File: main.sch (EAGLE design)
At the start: 12 parts, among them IC1 4001N, IC2 4069N, IC3 ISO1050DUB, IC4 ISO1050DUB, IC5 LD117AV33

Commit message: Pin pitch of TI's MSP430 N20 package now aligns with grid
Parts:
- renumbered 5V to VIN
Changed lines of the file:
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@@
 <part name="P+5" library="supply1" deviceset="VCC" device=""/>
 <part name="GND3" library="supply1" deviceset="GND" device=""/>
-<part name="5V" library="pinhead" deviceset="PINHD-1X2" device=""/>
+<part name="VIN" library="pinhead" deviceset="PINHD-1X2" device=""/>
 <part name="GND8" library="supply1" deviceset="GND" device=""/>
 <part name="GND10" library="supply1" deviceset="GND" device=""/>
@@
 <instance part="P+5" gate="VCC" x="48.26" y="78.74" rot="R180"/>
 <instance part="GND3" gate="1" x="48.26" y="91.44" rot="R180"/>
-<instance part="5V" gate="G$1" x="5.08" y="53.34" rot="R180"/>
+<instance part="VIN" gate="G$1" x="5.08" y="53.34" rot="R180"/>
 <instance part="GND8" gate="1" x="7.62" y="43.18"/>
 <instance part="IC2" gate="E" x="106.68" y="101.6" rot="R180"/>
@@
 </segment>
 <segment>
-<pinref part="5V" gate="G$1" pin="1"/>
+<pinref part="VIN" gate="G$1" pin="1"/>
 <pinref part="GND8" gate="1" pin="GND"/>
 <wire x1="7.62" y1="45.72" x2="7.62" y2="50.8" width="0.1524" layer="91"/>
@@
 <wire x1="15.24" y1="53.34" x2="17.78" y2="53.34" width="0.1524" layer="91"/>
 <junction x="15.24" y="53.34"/>
-<pinref part="5V" gate="G$1" pin="2"/>
-</segment>
-</net>
+<pinref part="VIN" gate="G$1" pin="2"/>
+</segment>
+</net>

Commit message: Replaced MSP430 with correct IC (MSP430G2553), improved board annotations, and added parts list to README
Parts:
- removed MSP430: G2X[0/3]2---N20, TI_MSP430_v16:G2X[0/3]2---N20
- added MSP430G2553: G2XX3---N20, TI_MSP430_v16:G2XX3---N20
- C1: value 100nf -> 0.1uF
- C2: value 10uf -> 10uF
- renumbered C3 to C1, C4 to C2, IC1 to RON, IC2 to VNI, IC3 to HVISO, IC4 to LVISO
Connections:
- net GND: now also MSP430G2553.20; no longer MSP430.20
- net N$1: now also MSP430G2553.16; no longer MSP430.16
- net N$2: now also MSP430G2553.17; no longer MSP430.17
- net N$21: now also MSP430G2553.8; no longer MSP430.8
- net N$22: now also MSP430G2553.13; no longer MSP430.13
- net N$24: now also MSP430G2553.9; no longer MSP430.9
- net N$25: now also MSP430G2553.12; no longer MSP430.12
- net VCC: now also MSP430G2553.1; no longer MSP430.1

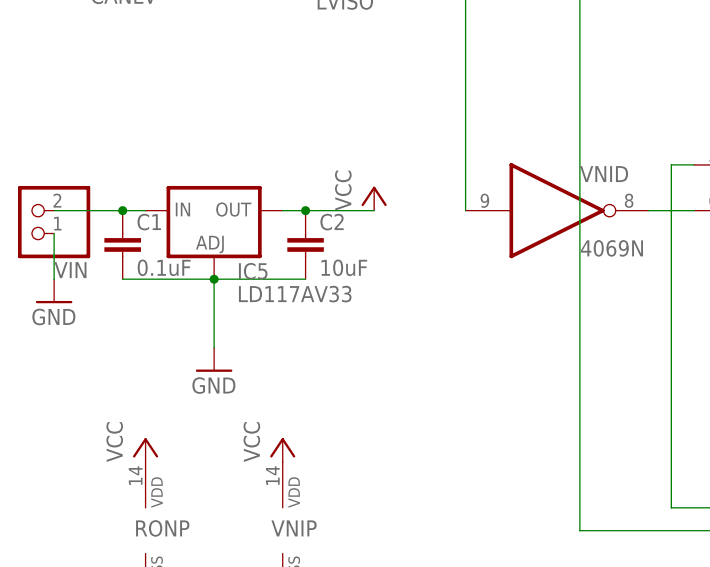
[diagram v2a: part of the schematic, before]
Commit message: PCB tweaks in pursuit of a planar design (not working)
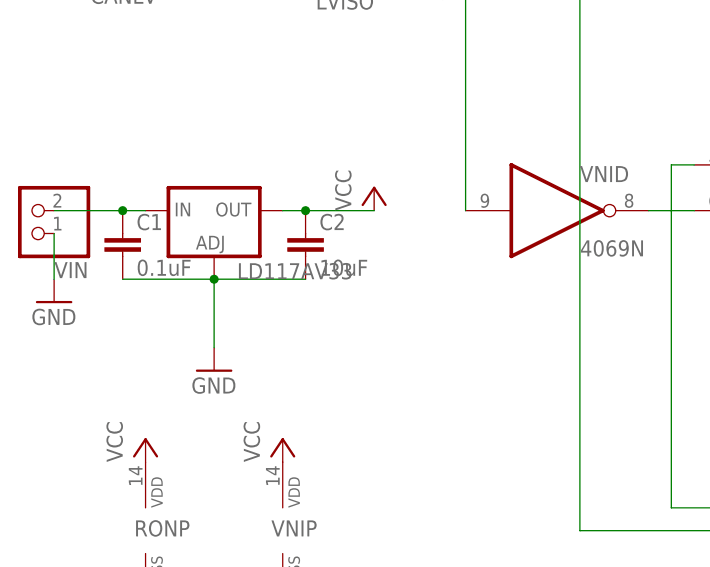
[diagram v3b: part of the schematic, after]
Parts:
- renumbered IC5 to LD117AV33
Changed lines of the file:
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@@
 <part name="HVISO" library="texas" deviceset="ISO1050" device="DUB" value=""/>
 <part name="LVISO" library="texas" deviceset="ISO1050" device="DUB" value=""/>
-<part name="IC5" library="v-reg" deviceset="LD117A?*" device="V" technology="33"/>
+<part name="LD117AV33" library="v-reg" deviceset="LD117A?*" device="V" technology="33" value=""/>
 <part name="P+1" library="supply1" deviceset="VCC" device=""/>
 <part name="GND1" library="supply1" deviceset="GND" device=""/>
@@
 <instance part="HVISO" gate="G$1" x="236.22" y="83.82"/>
 <instance part="LVISO" gate="G$1" x="33.02" y="83.82" rot="R180"/>
-<instance part="IC5" gate="G$1" x="25.4" y="53.34"/>
+<instance part="LD117AV33" gate="G$1" x="25.4" y="53.34"/>
 <instance part="P+1" gate="VCC" x="43.18" y="55.88"/>
 <instance part="GND1" gate="1" x="25.4" y="35.56"/>
@@
 <net name="VCC" class="0">
 <segment>
-<pinref part="IC5" gate="G$1" pin="OUT"/>
+<pinref part="LD117AV33" gate="G$1" pin="OUT"/>
 <pinref part="P+1" gate="VCC" pin="VCC"/>
 <wire x1="43.18" y1="53.34" x2="35.56" y2="53.34" width="0.1524" layer="91"/>
@@
 <net name="GND" class="0">
 <segment>
-<pinref part="IC5" gate="G$1" pin="ADJ"/>
+<pinref part="LD117AV33" gate="G$1" pin="ADJ"/>
 <pinref part="GND1" gate="1" pin="GND"/>
 <wire x1="25.4" y1="38.1" x2="25.4" y2="45.72" width="0.1524" layer="91"/>
@@
 <net name="N$23" class="0">
 <segment>
-<pinref part="IC5" gate="G$1" pin="IN"/>
+<pinref part="LD117AV33" gate="G$1" pin="IN"/>
 <wire x1="7.62" y1="53.34" x2="15.24" y2="53.34" width="0.1524" layer="91"/>
 <pinref part="C1" gate="G$1" pin="1"/>

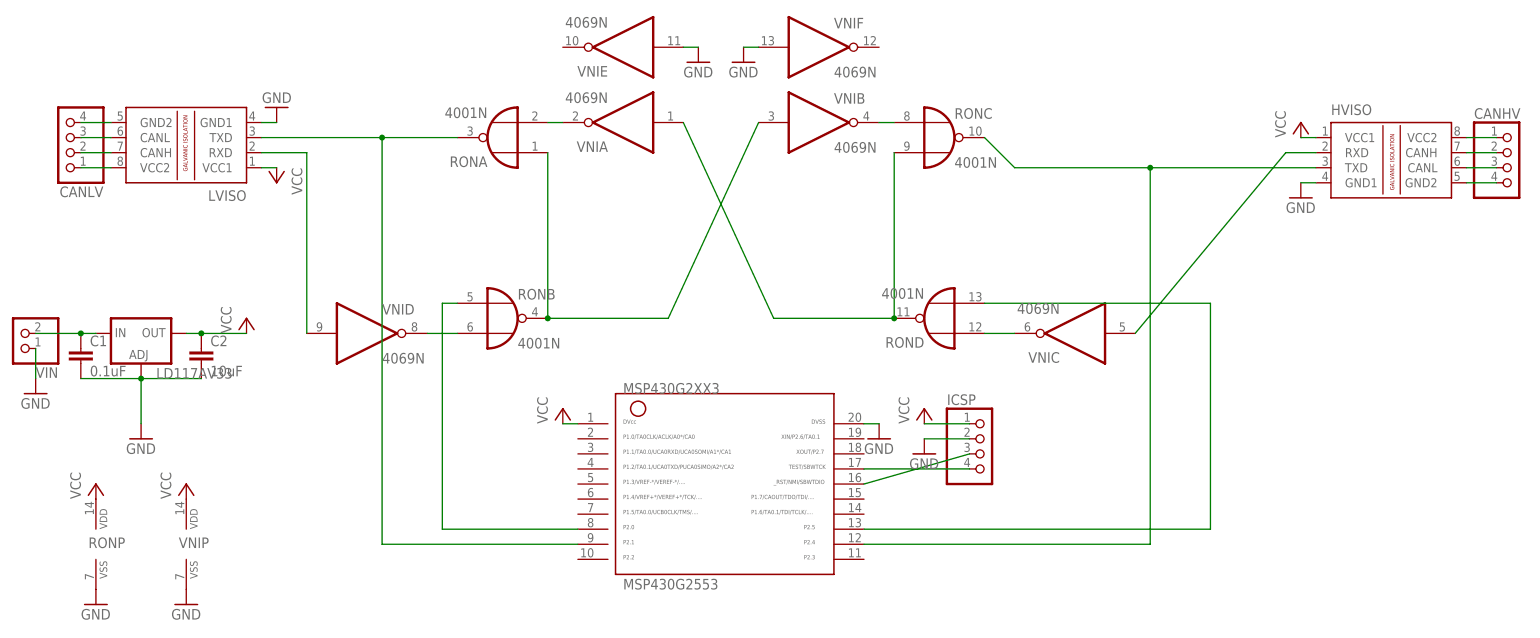
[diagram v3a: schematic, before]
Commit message: Rotated gates 90 CCW to achieve smaller board with much shorter traces
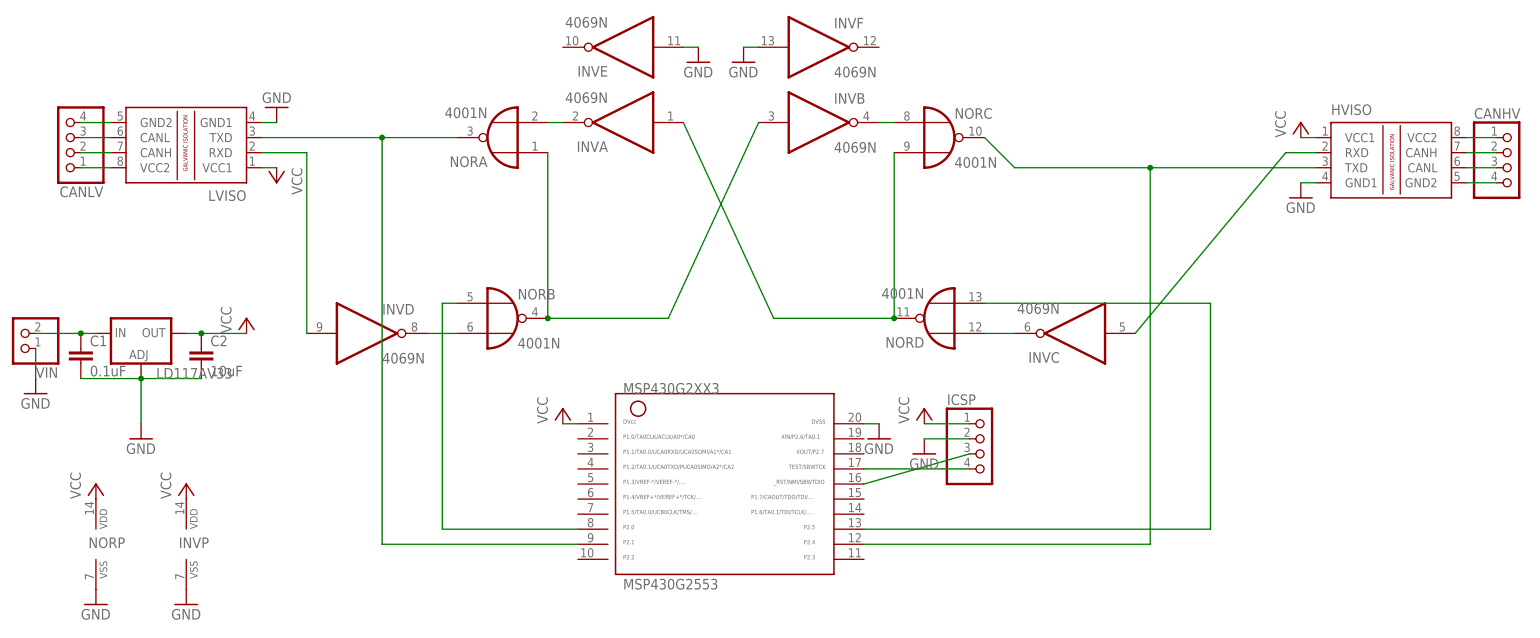
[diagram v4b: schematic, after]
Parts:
- renumbered RON to NOR, VNI to INV
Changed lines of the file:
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@@
 </classes>
 <parts>
-<part name="RON" library="40xx" deviceset="4001" device="N"/>
-<part name="VNI" library="40xx" deviceset="4069" device="N"/>
+<part name="NOR" library="40xx" deviceset="4001" device="N"/>
+<part name="INV" library="40xx" deviceset="4069" device="N"/>
 <part name="HVISO" library="texas" deviceset="ISO1050" device="DUB" value=""/>
 <part name="LVISO" library="texas" deviceset="ISO1050" device="DUB" value=""/>
@@
 </plain>
 <instances>
-<instance part="RON" gate="A" x="86.36" y="86.36" rot="R180"/>
-<instance part="RON" gate="B" x="86.36" y="55.88"/>
-<instance part="RON" gate="C" x="160.02" y="86.36"/>
-<instance part="RON" gate="D" x="160.02" y="55.88" rot="R180"/>
-<instance part="VNI" gate="A" x="106.68" y="88.9" rot="R180"/>
-<instance part="VNI" gate="B" x="139.7" y="88.9"/>
-<instance part="VNI" gate="C" x="182.88" y="53.34" rot="R180"/>
-<instance part="VNI" gate="D" x="63.5" y="53.34"/>
+<instance part="NOR" gate="A" x="86.36" y="86.36" rot="R180"/>
+<instance part="NOR" gate="B" x="86.36" y="55.88"/>
+<instance part="NOR" gate="C" x="160.02" y="86.36"/>
+<instance part="NOR" gate="D" x="160.02" y="55.88" rot="R180"/>
+<instance part="INV" gate="A" x="106.68" y="88.9" rot="R180"/>
+<instance part="INV" gate="B" x="139.7" y="88.9"/>
+<instance part="INV" gate="C" x="182.88" y="53.34" rot="R180"/>
+<instance part="INV" gate="D" x="63.5" y="53.34"/>
 <instance part="HVISO" gate="G$1" x="236.22" y="83.82"/>
 <instance part="LVISO" gate="G$1" x="33.02" y="83.82" rot="R180"/>
@@
 <instance part="P+1" gate="VCC" x="43.18" y="55.88"/>
 <instance part="GND1" gate="1" x="25.4" y="35.56"/>
-<instance part="RON" gate="P" x="17.78" y="17.78"/>
-<instance part="VNI" gate="P" x="33.02" y="17.78"/>
+<instance part="NOR" gate="P" x="17.78" y="17.78"/>
+<instance part="INV" gate="P" x="33.02" y="17.78"/>
 <instance part="P+2" gate="VCC" x="17.78" y="27.94"/>
 <instance part="P+3" gate="VCC" x="33.02" y="27.94"/>
@@
 <instance part="VIN" gate="G$1" x="5.08" y="53.34" rot="R180"/>
 <instance part="GND8" gate="1" x="7.62" y="43.18"/>
-<instance part="VNI" gate="E" x="106.68" y="101.6" rot="R180"/>
-<instance part="VNI" gate="F" x="139.7" y="101.6"/>
+<instance part="INV" gate="E" x="106.68" y="101.6" rot="R180"/>
+<instance part="INV" gate="F" x="139.7" y="101.6"/>
 <instance part="GND10" gate="1" x="119.38" y="99.06"/>
 <instance part="GND11" gate="1" x="127" y="99.06"/>
@@
 </segment>
 <segment>
-<pinref part="RON" gate="P" pin="VDD"/>
+<pinref part="NOR" gate="P" pin="VDD"/>
 <pinref part="P+2" gate="VCC" pin="VCC"/>
 </segment>
 <segment>
-<pinref part="VNI" gate="P" pin="VDD"/>
+<pinref part="INV" gate="P" pin="VDD"/>
 <pinref part="P+3" gate="VCC" pin="VCC"/>
 </segment>
@@
 </segment>
 <segment>
-<pinref part="RON" gate="P" pin="VSS"/>
+<pinref part="NOR" gate="P" pin="VSS"/>
 <pinref part="GND6" gate="1" pin="GND"/>
 </segment>
 <segment>
-<pinref part="VNI" gate="P" pin="VSS"/>
+<pinref part="INV" gate="P" pin="VSS"/>
 <pinref part="GND7" gate="1" pin="GND"/>
 </segment>
@@
 </segment>
 <segment>
-<pinref part="VNI" gate="E" pin="I"/>
+<pinref part="INV" gate="E" pin="I"/>
 <pinref part="GND10" gate="1" pin="GND"/>
 <wire x1="119.38" y1="101.6" x2="116.84" y2="101.6" width="0.1524" layer="91"/>
 </segment>
 <segment>
-<pinref part="VNI" gate="F" pin="I"/>
+<pinref part="INV" gate="F" pin="I"/>
 <pinref part="GND11" gate="1" pin="GND"/>
 <wire x1="127" y1="101.6" x2="129.54" y2="101.6" width="0.1524" layer="91"/>
@@
 <net name="N$3" class="0">
 <segment>
-<pinref part="RON" gate="B" pin="I1"/>
-<pinref part="VNI" gate="D" pin="O"/>
+<pinref part="NOR" gate="B" pin="I1"/>
+<pinref part="INV" gate="D" pin="O"/>
 <wire x1="73.66" y1="53.34" x2="78.74" y2="53.34" width="0.1524" layer="91"/>
 </segment>
@@
 <net name="N$4" class="0">
 <segment>
-<pinref part="RON" gate="A" pin="I1"/>
-<pinref part="VNI" gate="A" pin="O"/>
+<pinref part="NOR" gate="A" pin="I1"/>
+<pinref part="INV" gate="A" pin="O"/>
 <wire x1="96.52" y1="88.9" x2="93.98" y2="88.9" width="0.1524" layer="91"/>
 </segment>
@@
 <net name="N$5" class="0">
 <segment>
-<pinref part="RON" gate="C" pin="I0"/>
-<pinref part="VNI" gate="B" pin="O"/>
+<pinref part="NOR" gate="C" pin="I0"/>
+<pinref part="INV" gate="B" pin="O"/>
 <wire x1="149.86" y1="88.9" x2="152.4" y2="88.9" width="0.1524" layer="91"/>
 </segment>
@@
 <net name="N$6" class="0">
 <segment>
-<pinref part="RON" gate="D" pin="I0"/>
-<pinref part="VNI" gate="C" pin="O"/>
+<pinref part="NOR" gate="D" pin="I0"/>
+<pinref part="INV" gate="C" pin="O"/>
 <wire x1="172.72" y1="53.34" x2="167.64" y2="53.34" width="0.1524" layer="91"/>
 </segment>
@@
 <net name="N$7" class="0">
 <segment>
-<pinref part="RON" gate="D" pin="O"/>
-<pinref part="RON" gate="C" pin="I1"/>
+<pinref part="NOR" gate="D" pin="O"/>
+<pinref part="NOR" gate="C" pin="I1"/>
 <wire x1="152.4" y1="55.88" x2="152.4" y2="83.82" width="0.1524" layer="91"/>
-<pinref part="VNI" gate="A" pin="I"/>
+<pinref part="INV" gate="A" pin="I"/>
 <wire x1="152.4" y1="55.88" x2="132.08" y2="55.88" width="0.1524" layer="91"/>
 <wire x1="132.08" y1="55.88" x2="116.84" y2="88.9" width="0.1524" layer="91"/>
@@
 <net name="N$8" class="0">
 <segment>
-<pinref part="RON" gate="B" pin="O"/>
-<pinref part="VNI" gate="B" pin="I"/>
+<pinref part="NOR" gate="B" pin="O"/>
+<pinref part="INV" gate="B" pin="I"/>
 <wire x1="93.98" y1="55.88" x2="114.3" y2="55.88" width="0.1524" layer="91"/>
 <wire x1="114.3" y1="55.88" x2="129.54" y2="88.9" width="0.1524" layer="91"/>
-<pinref part="RON" gate="A" pin="I0"/>
+<pinref part="NOR" gate="A" pin="I0"/>
 <wire x1="93.98" y1="55.88" x2="93.98" y2="83.82" width="0.1524" layer="91"/>
 <junction x="93.98" y="55.88"/>
@@
 <net name="N$18" class="0">
 <segment>
-<pinref part="VNI" gate="C" pin="I"/>
+<pinref part="INV" gate="C" pin="I"/>
 <pinref part="HVISO" gate="G$1" pin="RXD"/>
 <wire x1="193.04" y1="53.34" x2="218.44" y2="83.82" width="0.1524" layer="91"/>
@@
 <net name="N$25" class="0">
 <segment>
-<pinref part="RON" gate="C" pin="O"/>
+<pinref part="NOR" gate="C" pin="O"/>
 <pinref part="HVISO" gate="G$1" pin="TXD"/>
 <wire x1="167.64" y1="86.36" x2="172.72" y2="81.28" width="0.1524" layer="91"/>
@@
 <net name="N$24" class="0">
 <segment>
-<pinref part="RON" gate="A" pin="O"/>
+<pinref part="NOR" gate="A" pin="O"/>
 <pinref part="LVISO" gate="G$1" pin="TXD"/>
 <wire x1="78.74" y1="86.36" x2="66.04" y2="86.36" width="0.1524" layer="91"/>
@@
 <segment>
 <pinref part="LVISO" gate="G$1" pin="RXD"/>
-<pinref part="VNI" gate="D" pin="I"/>
+<pinref part="INV" gate="D" pin="I"/>
 <wire x1="45.72" y1="83.82" x2="53.34" y2="83.82" width="0.1524" layer="91"/>
 <wire x1="53.34" y1="83.82" x2="53.34" y2="53.34" width="0.1524" layer="91"/>
@@
 <net name="N$21" class="0">
 <segment>
-<pinref part="RON" gate="B" pin="I0"/>
+<pinref part="NOR" gate="B" pin="I0"/>
 <wire x1="99.06" y1="20.32" x2="76.2" y2="20.32" width="0.1524" layer="91"/>
 <wire x1="76.2" y1="20.32" x2="76.2" y2="58.42" width="0.1524" layer="91"/>
@@
 <net name="N$22" class="0">
 <segment>
-<pinref part="RON" gate="D" pin="I1"/>
+<pinref part="NOR" gate="D" pin="I1"/>
 <wire x1="147.32" y1="20.32" x2="205.74" y2="20.32" width="0.1524" layer="91"/>
 <wire x1="167.64" y1="58.42" x2="205.74" y2="58.42" width="0.1524" layer="91"/>
